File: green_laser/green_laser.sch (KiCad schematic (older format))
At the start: 14 parts, among them Q1 2X, Q2 491, Q3 Q_Photo_NPN, SW1 SW_Push

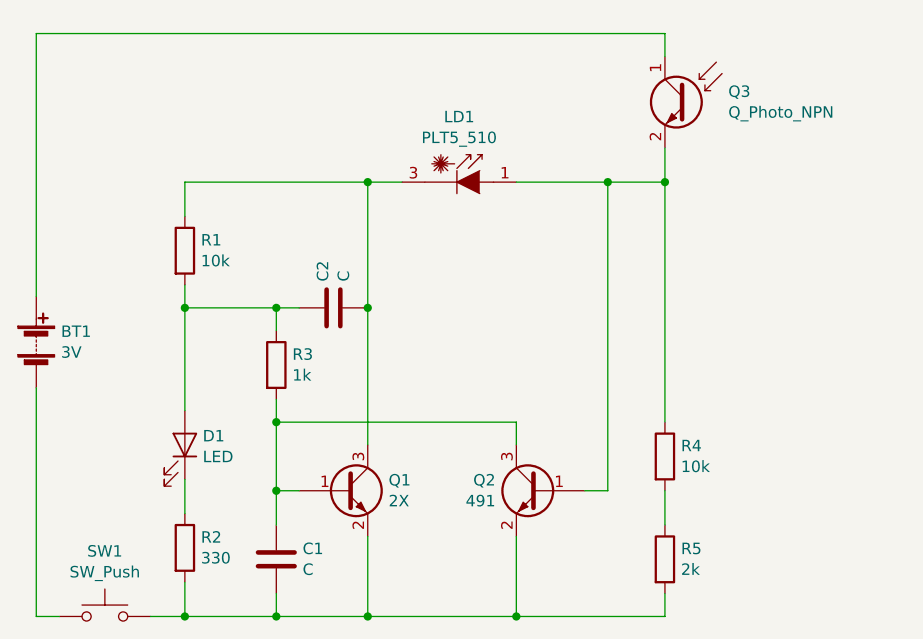
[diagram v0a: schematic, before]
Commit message: fixed V+ on schematic
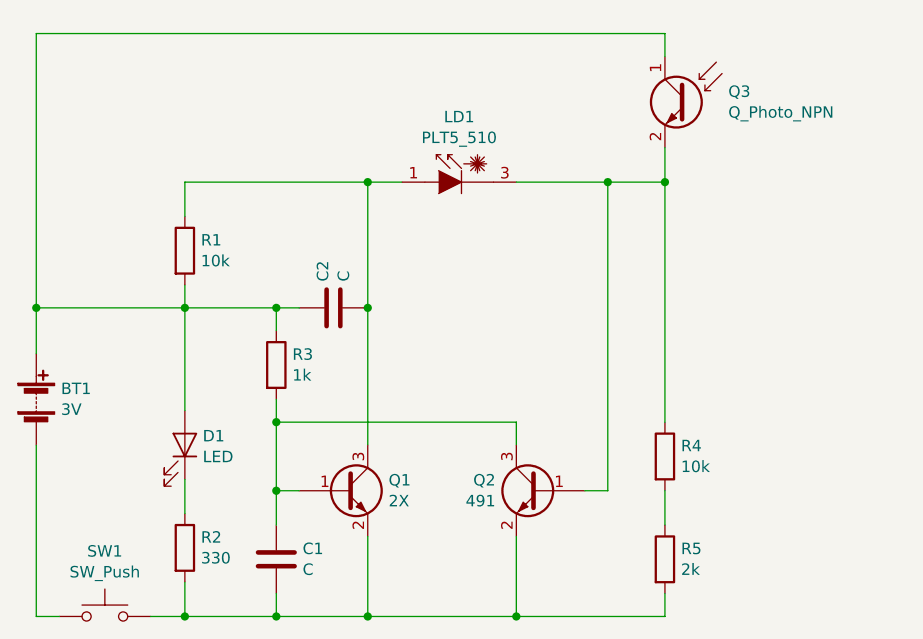
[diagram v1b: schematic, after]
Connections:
- net at Q2.1 (B), Q3.2 (E), R4.1: now also LD1.3 (C); no longer LD1.1 (A)
- net at C2.2, Q1.3 (C), R1.1: now also LD1.1 (A); no longer LD1.3 (C)
- net at BT1.1 (+), Q3.1 (C): now also C2.1, D1.2 (A), R1.2, R3.1
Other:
- moved on the sheet: BT1
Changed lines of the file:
@@
 L Device:Battery BT1
 U 1 1 5D33944D
-P 2450 3650
-F 0 "BT1" H 2558 3696 50  0000 L CNN
-F 1 "3V" H 2558 3605 50  0000 L CNN
-F 2 "" V 2450 3710 50  0001 C CNN
-F 3 "~" V 2450 3710 50  0001 C CNN
-	1    2450 3650
+P 2450 3900
+F 0 "BT1" H 2558 3946 50  0000 L CNN
+F 1 "3V" H 2558 3855 50  0000 L CNN
+F 2 "" V 2450 3960 50  0001 C CNN
+F 3 "~" V 2450 3960 50  0001 C CNN
+	1    2450 3900
 	1    0    0    -1
 $EndComp
@@
 L Diode_Laser:PLT5_510 LD1
 U 1 1 5D341E96
-P 4350 2950
-F 0 "LD1" H 4300 3235 50  0000 C CNN
-F 1 "PLT5_510" H 4300 3144 50  0000 C CNN
-F 2 "OptoDevice:LaserDiode_TO38ICut-3" H 4350 2775 50  0001 C CNN
-F 3 "http://www.osram-os.com/Graphics/XPic2/00227065_0.pdf/PLT5%20510.pdf" H 4380 2750 50  0001 C CNN
-	1    4350 2950
-	1    0    0    -1
+P 4250 2950
+F 0 "LD1" H 4200 3235 50  0000 C CNN
+F 1 "PLT5_510" H 4200 3144 50  0000 C CNN
+F 2 "OptoDevice:LaserDiode_TO38ICut-3" H 4250 2775 50  0001 C CNN
+F 3 "http://www.osram-os.com/Graphics/XPic2/00227065_0.pdf/PLT5%20510.pdf" H 4280 2750 50  0001 C CNN
+	1    4250 2950
+	-1   0    0    -1
 $EndComp
 $Comp
@@
 $EndComp
 Wire Wire Line
-	2450 3850 2450 4850
+	2450 4100 2450 4850
 Wire Wire Line
 	2450 4850 2550 4850
 Wire Wire Line
-	2450 2300 2450 3450
+	2450 2300 2450 3500
 $Comp
 L Device:R R3
@@
 	5200 2800 5200 2950
 Connection ~ 5200 2950
+Wire Wire Line
+	3100 3500 2450 3500
+Connection ~ 2450 3500
+Wire Wire Line
+	2450 3500 2450 3700
 $EndSCHEMATC

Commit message: updated schematic based on forum feedback
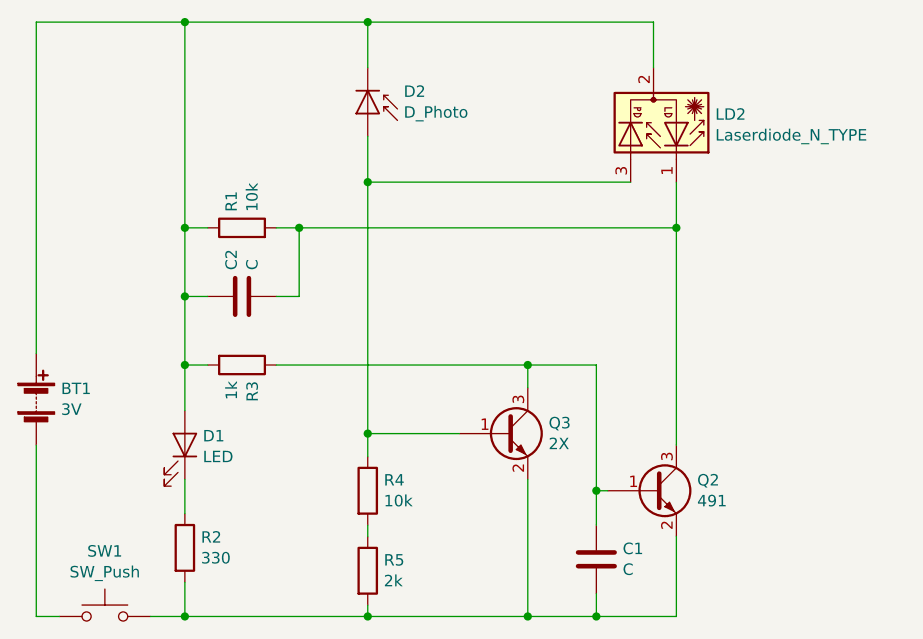
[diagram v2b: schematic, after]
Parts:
- removed LD1: PLT5_510, OptoDevice:LaserDiode_TO38ICut-3, symbol Diode_Laser:PLT5_510
- removed Q1: 2X, symbol Device:Q_NPN_BEC
- removed Q3: Q_Photo_NPN, symbol Device:Q_Photo_NPN
- added D2: D_Photo, symbol Device:D_Photo
- added LD2: Laserdiode_N_TYPE, symbol Device:Laserdiode_N_TYPE
- added Q3: 2X, symbol Device:Q_NPN_BEC
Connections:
- net at Q2.1 (B): now also C1.1, R3.1, Q3.3 (C); no longer R4.1
- net at C1.2, Q2.2 (E), R2.2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: now also Q3.2 (E)
- net at C2.2: now also Q2.3 (C), R1.2, LD2.1; no longer R1.1
- net at BT1.1 (+), C2.1, D1.2 (A): now also R1.1, R3.2, D2.1 (K), LD2.2; no longer R1.2, R3.1
- new net: D2.2 (A), LD2.3, Q3.1 (B), R4.1
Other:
- moved on the sheet: C1, C2, Q2, R1, R3
